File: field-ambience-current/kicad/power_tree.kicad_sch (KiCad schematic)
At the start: 19 parts, among them J1 USB_C_Receptacle (TYPE-C-31-M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, U5 AP7361C-33 1A LDO (+5V->+3V3,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

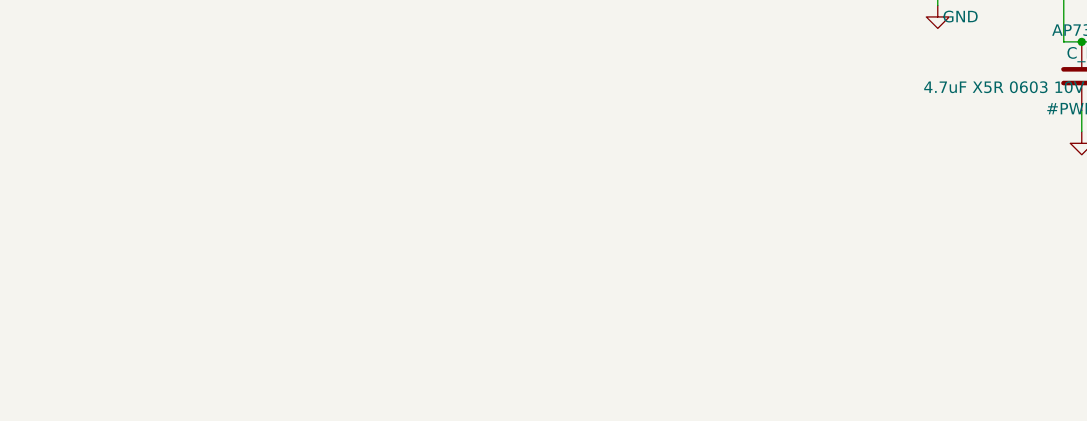
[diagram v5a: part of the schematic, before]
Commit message: fix(pcb): both PCA9685 /OE pull-ups had no driver — LEDs would never light; +mounting holes +test points +cost estimate (r18.84)
User asked whether any must-have components are missing, and for a fresh
JLC cost estimate.

CRITICAL find: both PCA9685 output-enable pins (R_OE on U6, R_OE2 on U10)
were pulled HIGH to +3V3 with a comment claiming firmware drives /OE low
after PWM init — but no net connected /OE to any MCU/MCP pin, so nothing
could ever drive it. /OE would sit HIGH forever: all 15 status LEDs, the
LCD backlight AND the 8 VU LEDs permanently disabled (backlight off = the
screen is unreadable). Fixed to pull-DOWN (outputs always enabled).
Boot-dark is still guaranteed by the chip itself: NXP datasheet Table 7,
LEDn_OFF_H[4] 'full OFF' defaults to 1 on every channel, verified against
the PDF — the part powers up with every channel in FULL_OFF regardless of
/OE. Firmware pca_init comments updated to match (nothing to sequence).

Added missing must-haves:
- 4x M2.5 mounting holes H1-H4 (plated, GND) — defined in the mechanical
  spec section 6 all along ((12,6)/(240,6)/(12,96)/(240,96)) but never in
  the schematic. DNP symbols with footprint MountingHole_2.7mm_M2.5_Pad
  (FP note: KiCad's 5.4mm pad vs the spec's 6mm — a layout call for Aron).
- 7 test points (AI_READY schematic standard requires TP_*): TP_5V,
  TP_3V3, TP_5VSW, TP_VBUS, TP_GND1/2 on power_tree + TP_BAT on battery,
  all DNP TestPoint_Pad_D1.5mm.
Both are fit-free, so jlc_bom.csv is unchanged at 58 parts / 210
placements (the exporter correctly skips the 11 DNP items).

Completeness sweep otherwise clean: USB protection (fuse+TVS+ESD+CC),
charge/power path incl. on/off (since r18.81), NRST/BOOT0, VCAP, HSE +
loads, I2C pull-ups, status LED, backlight driver, SWD, jack clamp
(r18.82). Deliberately NOT on the PCB (not defects): battery protection
PCM (must live in the LiPo pouch — buy note added), fiducials (JLC adds
them at panelization), MIDI-IN (OUT only per ADR-0004).

Cost estimate rebuilt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
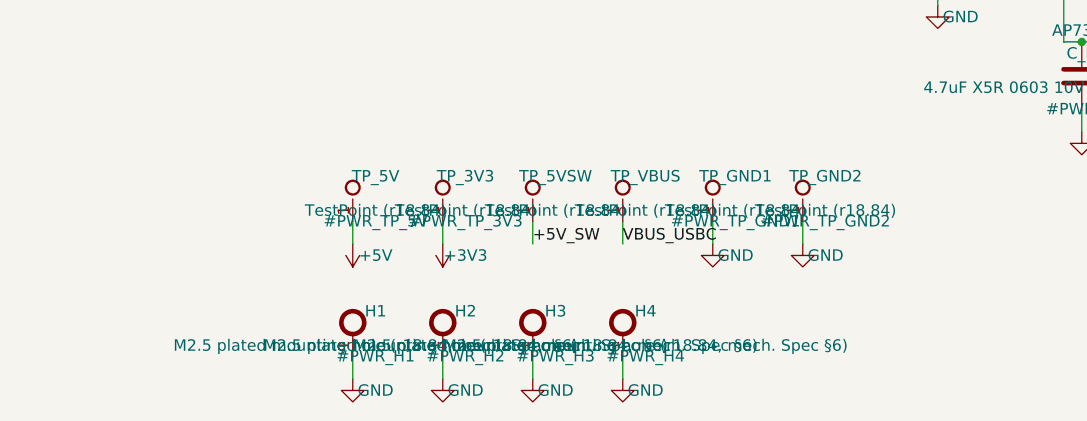
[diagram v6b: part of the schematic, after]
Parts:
- added H1, H2, H3, H4: M2.5 plated mounting hole (r18.84, mech. Spec §6), MountingHole:MountingHole_2.7mm_M2.5_Pad, symbol Mechanical:MountingHole_Pad
- added TP_3V3, TP_5V, TP_5VSW, TP_GND1, TP_GND2, TP_VBUS: TestPoint (r18.84), TestPoint:TestPoint_Pad_D1.5mm, symbol Connector:TestPoint
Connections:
- net +3V3: now also TP_3V3.1
- net +5V: now also TP_5V.1
- net +5V_SW: now also TP_5VSW.1
- net +5V_USB: now also TP_VBUS.1
- net GND: now also H1.1, H2.1, H3.1, H4.1, TP_GND1.1, TP_GND2.1

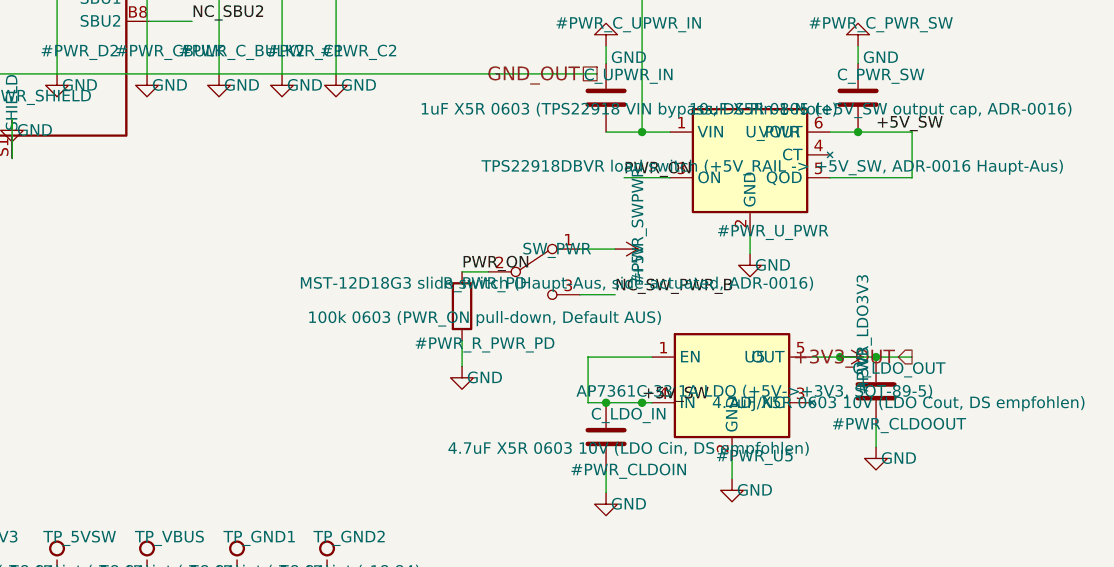
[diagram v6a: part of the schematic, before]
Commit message: pcb(power): SW_PWR premium swap — ALPS SSSS811101 (TE-grade), datasheet-verified side actuation (r18.85)
User direction: high-quality on/off slider like Teenage Engineering, JLC/LCSC-
sourced, natively side-actuated (no motion-redirecting cap mechanics).

- SW_PWR: MST-12D18G3 (SHOU HAN, budget) -> ALPS ALPINE SSSS811101, C109335,
  JLC Extended ~33k stock, ~$0.15. ALPS datasheet verified: 'Actuator
  directions: Horizontal' — knob protrudes sideways, slides parallel to the
  board; same-axis cap engagement, no redirection (the user's concern).
- Footprint vendored via easyeda2kicad (repo method) as
  field_ambience:SW_ALPS-SSSS811101_SlideSwitch_SMD + STEP, and verified
  against the ALPS land pattern p.3: 3 signal pads 0.7mm @ 3.0/1.5mm asym
  pitch + 4 ground-frame pads 0.8x1.0 @ +-3.65mm + 2 locator holes o0.9 @
  3.0mm — exact match. Ground pads 4-7 solder-anchor the frame (not in the
  3-pin symbol; optional GND tie in layout).
- Bonus: common terminal is LABELED in the ALPS circuit diagram (C = term 2) —
  closes the MST 'terminals unlabeled / UNVERIFIED' gap from r18.81.
- Mechanical delta documented (BOM, MECHANICAL_REQUIREMENTS, Aron HTML): body
  only 1.4mm tall -> stem window z ~ 0-1.4mm above PCB (old MST 2.3-3.8mm);
  case slot + slider-cap finger must reach near board level.
- Aron HTML: SW_PWR row updated; STALE paragraph fixed ('power-off block = GUI
  drop-in' -> it is wired in power_tree since r18.81); custom-footprint list 9.
- MST-12D18G3 + its footprint stay vendored as documented budget fallback.
- Regenerated .kicad_sch + jlc_bom.csv (C109335 in, C49023766 out);
  check_pinmap green.

Co-Authored-By: Claude Fable 5 <noreply@anthropic.com>
Claude-Session: https://claude.ai/code/session_01K5kLTFpDCCoYwx2dq6RkAv
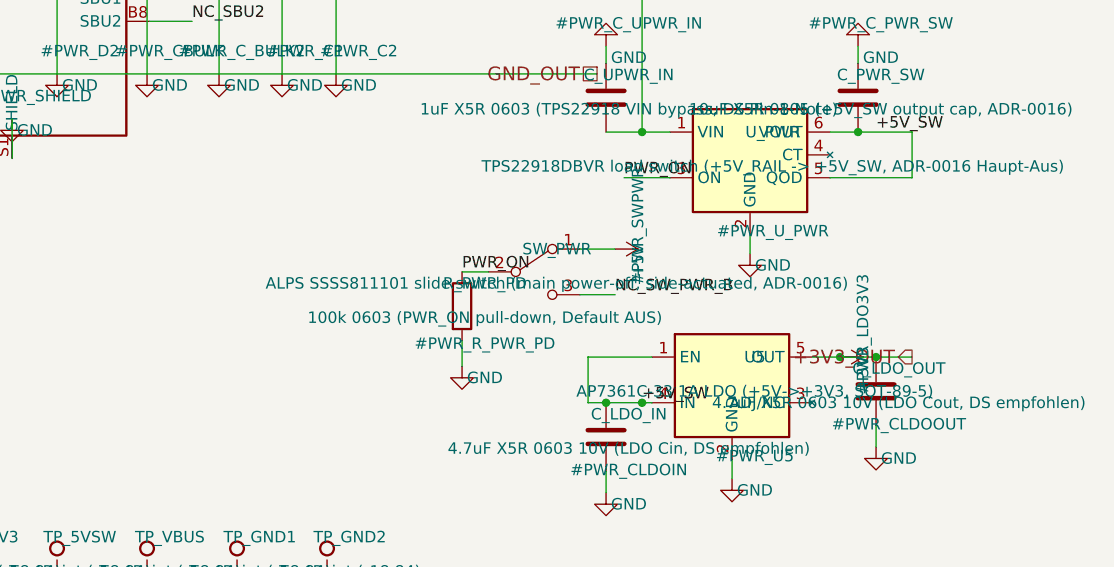
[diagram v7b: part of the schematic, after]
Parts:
- SW_PWR: value MST-12D18G3 slide switch (Haupt-Aus, side-actuated, ADR-0016) -> ALPS SSSS811101 slide switch (main power-off, side-actuated, ADR-0016); footprint field_ambience:SW_MST-12D18_SlideSwitch_RA -> field_ambience:SW_ALPS-SSSS811101_SlideSwitch_SMD; FP_NOTE r18.81 GEGEN DATENBLATT VERIFIZIERT: Land-Pattern MSK12D = 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 -> r18.85 GEGEN DATENBLATT VERIFIZIERT (ALPS Land Dimensions, 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; LCSC C49023766 -> C109335; MPN MST-12D18G3 -> SSSS811101; Manufacturer SHOU HAN -> ALPS ALPINE; PIN_NOTE UNVERIFIED — NEEDS HUMAN CHECK: Common = MITTELPAD angenomm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 -> Common = Terminal 2 — im ALPS-Schaltbild GELABELT (C), ande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; PREV_PART (none) -> MST-12D18G3 (SHOU HAN, C49023766) — Budget-Fallback; Footpr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
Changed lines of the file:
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@@
       (property "Reference" "SW_PWR" (at 110.54 115.46 0)
         (effects (font (size 1.27 1.27))))
-      (property "Value" "MST-12D18G3 slide switch (Haupt-Aus, side-actuated, ADR-0016)" (at 110.54 119.27 0)
+      (property "Value" "ALPS SSSS811101 slide switch (main power-off, side-actuated, ADR-0016)" (at 110.54 119.27 0)
         (effects (font (size 1.27 1.27))))
-      (property "Footprint" "field_ambience:SW_MST-12D18_SlideSwitch_RA" (at 108.0 118.0 0)
+      (property "Footprint" "field_ambience:SW_ALPS-SSSS811101_SlideSwitch_SMD" (at 108.0 118.0 0)
         (effects (font (size 1.27 1.27)) hide))
-      (property "Datasheet" "https://datasheet.lcsc.com/datasheet/pdf/8888d0ec4d46a4f060de0c433f52f277.pdf" (at 108.0 118.0 0)
+      (property "Datasheet" "https://wmsc.lcsc.com/wmsc/upload/file/pdf/v2/lcsc/1808041445_ALPSALPINE-SSSS811101_C109335.pdf" (at 108.0 118.0 0)
         (effects (font (size 1.27 1.27)) hide))
-      (property "MPN" "MST-12D18G3" (at 110.54 121.81 0)
+      (property "MPN" "SSSS811101" (at 110.54 121.81 0)
         (effects (font (size 1.27 1.27)) hide))
-      (property "Manufacturer" "SHOU HAN" (at 110.54 123.08 0)
+      (property "Manufacturer" "ALPS ALPINE" (at 110.54 123.08 0)
         (effects (font (size 1.27 1.27)) hide))
-      (property "LCSC" "C49023766" (at 110.54 124.35 0)
+      (property "LCSC" "C109335" (at 110.54 124.35 0)
         (effects (font (size 1.27 1.27)) hide))
-      (property "FP_NOTE" "r18.81 GEGEN DATENBLATT VERIFIZIERT: Land-Pattern MSK12D = 3 Pads 1,2 mm @ 2,5 mm Pitch + 2 Loecher Ø0,9 @ 6,8 mm, Pad-Mitte 3,2 mm (=2,1+2,2/2) von der Lochlinie — vendored Footprint stimmt exakt. Body flach auf der (horizontalen) PCB, Stem parallel zur PCB 3 mm ueber Body-Kante → am Board-Rand platzieren, Stem durch Slot in der Gehaeuse-Seitenwand." (at 110.54 125.62 0)
+      (property "FP_NOTE" "r18.85 GEGEN DATENBLATT VERIFIZIERT (ALPS Land Dimensions, S.3): 3 Signal-Pads 0,7 mm breit @ asymm. 3,0/1,5 mm Teilung + 4 Ground-Frame-Pads 0,8x1,0 @ +-3,65 mm (innere Kante 6,3 mm) + 2 Locator-Loecher O0,9 @ 3,0 mm — vendored Footprint (easyeda2kicad C109335) stimmt exakt. Body flach auf der PCB, Aktuator HORIZONTAL seitlich raus -> Board-Rand, Slot in der Gehaeuse-Seitenwand (z nahe PCB-Level!). Ground-Pads 4-7 sind nicht im 3-Pin-Symbol: loeten verankert den Metallrahmen; optional im Layout auf GND legen (EMC)." (at 110.54 125.62 0)
         (effects (font (size 1.27 1.27)) hide))
-      (property "PIN_NOTE" "UNVERIFIED — NEEDS HUMAN CHECK: Common = MITTELPAD angenommen (1P2T-Schiebeschalter-Konvention); das SHOU-HAN-DB labelt die Terminals nicht — vor Fab am Teil durchpiepen. Falsch-Fall waere fail-safe: Geraet liesse sich nur nicht einschalten (PWR_ON floatet nie: 100k-PD)." (at 110.54 126.89 0)
+      (property "PIN_NOTE" "Common = Terminal 2 — im ALPS-Schaltbild GELABELT (C), anders als beim frueheren MST (unlabeled). Kurzer Durchpiep-Check am physischen Teil vor Fab bleibt guenstige Absicherung; Falsch-Fall fail-safe (100k-PD haelt PWR_ON low)." (at 110.54 126.89 0)
+        (effects (font (size 1.27 1.27)) hide))
+      (property "PREV_PART" "MST-12D18G3 (SHOU HAN, C49023766) — Budget-Fallback; Footprint SW_MST-12D18_SlideSwitch_RA bleibt vendored im Repo." (at 110.54 128.16 0)
         (effects (font (size 1.27 1.27)) hide))
     (instances
